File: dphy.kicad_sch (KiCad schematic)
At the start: 5 parts, among them J1002 FFC-22p-P0.5mm, U1002 RCLAMP0524P, U1003 RCLAMP0524P, U1004 RCLAMP0524P, U1005 RCLAMP0524P

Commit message: Fix schematic ERC errors
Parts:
- U1002, U1003, U1004, U1005: footprint Package_SON:USON-10_2.5x1.0mm_P0.5mm -> Package_DFN_QFN:Diodes_UDFN-10_1.0x2.5mm_P0.5mm; symbol Yellow:TPD4EUSB30 -> Hatlabs:RCLAMP0524P
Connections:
- net +3.3V: no longer U1005.7 (D2+)
- net CAM_GPIO0: no longer U1004.7 (D2+)
- net CAM_GPIO1: no longer U1004.6 (D2-)
- net DPHY.C+: no longer U1003.10 (D1+)
- net DPHY.C-: no longer U1003.9 (D1-)
- net DPHY.D0+: no longer U1002.10 (D1+)
- net DPHY.D0-: no longer U1002.9 (D1-)
- net DPHY.D1+: no longer U1002.7 (D2+)
- net DPHY.D1-: no longer U1002.6 (D2-)
- net DPHY.D2+: no longer U1003.7 (D2+)
- net DPHY.D2-: no longer U1003.6 (D2-)
- net DPHY.D3+: no longer U1004.10 (D1+)
- net DPHY.D3-: no longer U1004.9 (D1-)
- net I2C.SCL: no longer U1005.10 (D1+)
- net I2C.SDA: no longer U1005.9 (D1-)
- net at U1005.5: no longer U1005.6 (D2-)
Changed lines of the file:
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@@
 	)
 	(symbol
-		(lib_name "Power_Protection:TPD4EUSB30_1")
-		(lib_id "Yellow:TPD4EUSB30")
+		(lib_id "Hatlabs:RCLAMP0524P")
 		(at 90.17 138.43 0)
 		(unit 1)
@@
 			)
 		)
-		(property "Footprint" "Package_SON:USON-10_2.5x1.0mm_P0.5mm"
+		(property "Footprint" "Package_DFN_QFN:Diodes_UDFN-10_1.0x2.5mm_P0.5mm"
 			(at 66.04 148.59 0)
 			(effects
@@
 			)
 		)
-		(property "Description" ""
+		(property "Description" "4-Channel Low Capacitance TVS Diode Array, DFN-10"
 			(at 90.17 138.43 0)
 			(effects
@@
 					(size 1.27 1.27)
 				)
-			)
-		)
-		(property "Sim.Enable" ""
-			(at 90.17 138.43 0)
-			(effects
-				(font
-					(size 1.27 1.27)
-				)
+				(hide yes)
 			)
 		)
@@
 	)
 	(symbol
-		(lib_name "Power_Protection:TPD4EUSB30_1")
-		(lib_id "Yellow:TPD4EUSB30")
+		(lib_id "Hatlabs:RCLAMP0524P")
 		(at 90.17 73.66 0)
 		(unit 1)
@@
 			)
 		)
-		(property "Footprint" "Package_SON:USON-10_2.5x1.0mm_P0.5mm"
+		(property "Footprint" "Package_DFN_QFN:Diodes_UDFN-10_1.0x2.5mm_P0.5mm"
 			(at 66.04 83.82 0)
 			(effects
@@
 			)
 		)
-		(property "Description" ""
+		(property "Description" "4-Channel Low Capacitance TVS Diode Array, DFN-10"
 			(at 90.17 73.66 0)
 			(effects
@@
 					(size 1.27 1.27)
 				)
-			)
-		)
-		(property "Sim.Enable" ""
-			(at 90.17 73.66 0)
-			(effects
-				(font
-					(size 1.27 1.27)
-				)
+				(hide yes)
 			)
 		)
@@
 	)
 	(symbol
-		(lib_name "Power_Protection:TPD4EUSB30_1")
-		(lib_id "Yellow:TPD4EUSB30")
+		(lib_id "Hatlabs:RCLAMP0524P")
 		(at 90.17 41.91 0)
 		(unit 1)
@@
 			)
 		)
-		(property "Footprint" "Package_SON:USON-10_2.5x1.0mm_P0.5mm"
+		(property "Footprint" "Package_DFN_QFN:Diodes_UDFN-10_1.0x2.5mm_P0.5mm"
 			(at 66.04 52.07 0)
 			(effects
@@
 			)
 		)
-		(property "Description" ""
+		(property "Description" "4-Channel Low Capacitance TVS Diode Array, DFN-10"
 			(at 90.17 41.91 0)
 			(effects
@@
 					(size 1.27 1.27)
 				)
-			)
-		)
-		(property "Sim.Enable" ""
-			(at 90.17 41.91 0)
-			(effects
-				(font
-					(size 1.27 1.27)
-				)
+				(hide yes)
 			)
 		)
@@
 			)
 		)
-		(property "Sim.Enable" ""
-			(at 214.63 91.44 0)
-			(effects
-				(font
-					(size 1.27 1.27)
-				)
-			)
-		)
 		(pin "1"
 		)
@@
 	)
 	(symbol
-		(lib_name "Power_Protection:TPD4EUSB30_1")
-		(lib_id "Yellow:TPD4EUSB30")
+		(lib_id "Hatlabs:RCLAMP0524P")
 		(at 90.17 106.68 0)
 		(unit 1)
@@
 			)
 		)
-		(property "Footprint" "Package_SON:USON-10_2.5x1.0mm_P0.5mm"
+		(property "Footprint" "Package_DFN_QFN:Diodes_UDFN-10_1.0x2.5mm_P0.5mm"
 			(at 66.04 116.84 0)
 			(effects
@@
 			)
 		)
-		(property "Description" ""
+		(property "Description" "4-Channel Low Capacitance TVS Diode Array, DFN-10"
 			(at 90.17 106.68 0)
 			(effects
@@
 					(size 1.27 1.27)
 				)
-			)
-		)
-		(property "Sim.Enable" ""
-			(at 90.17 106.68 0)
-			(effects
-				(font
-					(size 1.27 1.27)
-				)
-			)
-		)
+				(hide yes)
+			)
+		)

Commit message: Renumber all sheets
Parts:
- renumbered J1002 to J3401, U1003 to U3401, U1004 to U3402, U1005 to U3403, U1002 to U3404
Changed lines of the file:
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@@
 		(on_board yes)
 		(dnp no)
-		(property "Reference" "#PWR01014"
+		(property "Reference" "#PWR03402"
 			(at 207.01 127 0)
 			(effects
@@
 		(on_board yes)
 		(dnp no)
-		(property "Reference" "#PWR01010"
+		(property "Reference" "#PWR03405"
 			(at 90.17 92.71 0)
 			(effects
@@
 		(on_board yes)
 		(dnp no)
-		(property "Reference" "#PWR01009"
+		(property "Reference" "#PWR03404"
 			(at 90.17 60.96 0)
 			(effects
@@
 		(on_board yes)
 		(dnp no)
-		(property "Reference" "U1005"
+		(property "Reference" "U3403"
 			(at 90.17 125.73 0)
 			(effects
@@
 		(dnp no)
 		(fields_autoplaced yes)
-		(property "Reference" "#PWR01013"
+		(property "Reference" "#PWR01017"
 			(at 104.14 138.43 0)
 			(effects
@@
 		(on_board yes)
 		(dnp no)
-		(property "Reference" "U1003"
+		(property "Reference" "U3401"
 			(at 90.17 60.96 0)
 			(effects
@@
 		(on_board yes)
 		(dnp no)
-		(property "Reference" "#PWR01011"
+		(property "Reference" "#PWR03406"
 			(at 90.17 125.73 0)
 			(effects
@@
 		(on_board yes)
 		(dnp no)
-		(property "Reference" "#PWR01012"
+		(property "Reference" "#PWR03407"
 			(at 90.17 157.48 0)
 			(effects
@@
 		(on_board yes)
 		(dnp no)
-		(property "Reference" "U1002"
+		(property "Reference" "U3404"
 			(at 90.17 29.21 0)
 			(effects
@@
 		(on_board yes)
 		(dnp no)
-		(property "Reference" "#PWR01015"
+		(property "Reference" "#PWR03403"
 			(at 214.63 130.81 0)
 			(effects
@@
 		(dnp no)
 		(fields_autoplaced yes)
-		(property "Reference" "J1002"
+		(property "Reference" "J3401"
 			(at 217.17 91.7955 0)
 			(effects
@@
 					(size 1.27 1.27)
 				)
+				(hide yes)
 			)
 		)
@@
 		(on_board yes)
 		(dnp no)
-		(property "Reference" "U1004"
+		(property "Reference" "U3402"
 			(at 90.17 93.98 0)
 			(effects
@@
 		(dnp no)
 		(fields_autoplaced yes)
-		(property "Reference" "#PWR01003"
+		(property "Reference" "#PWR03408"
 			(at 186.69 123.19 0)
 			(effects

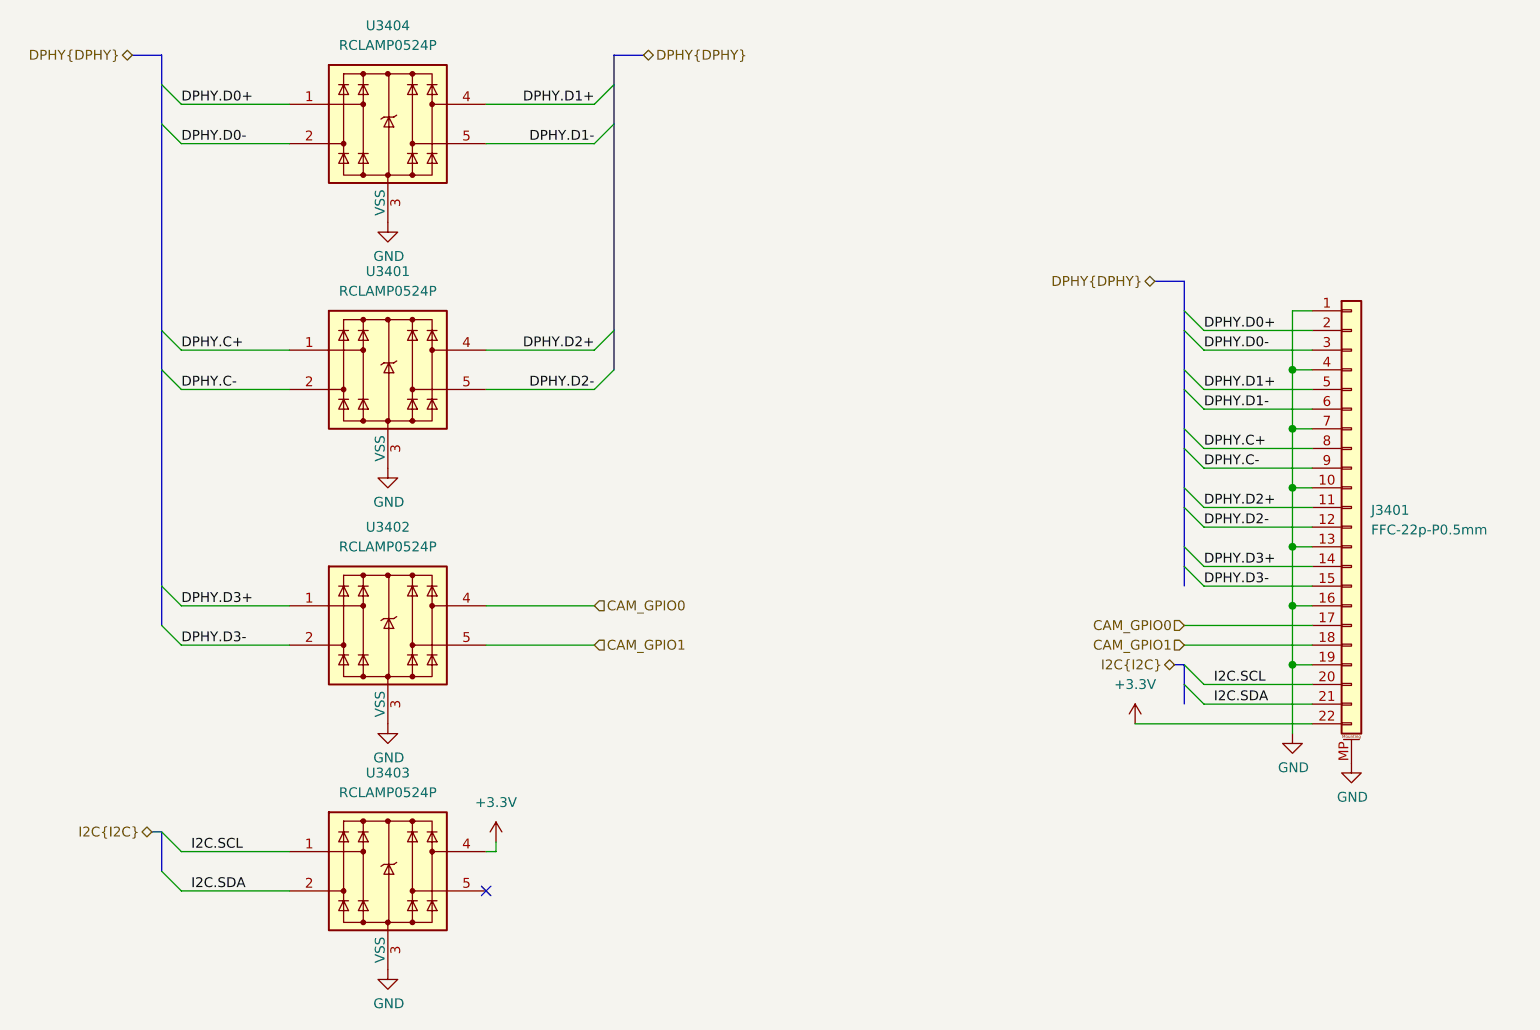
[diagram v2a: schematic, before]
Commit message: Reannotate components
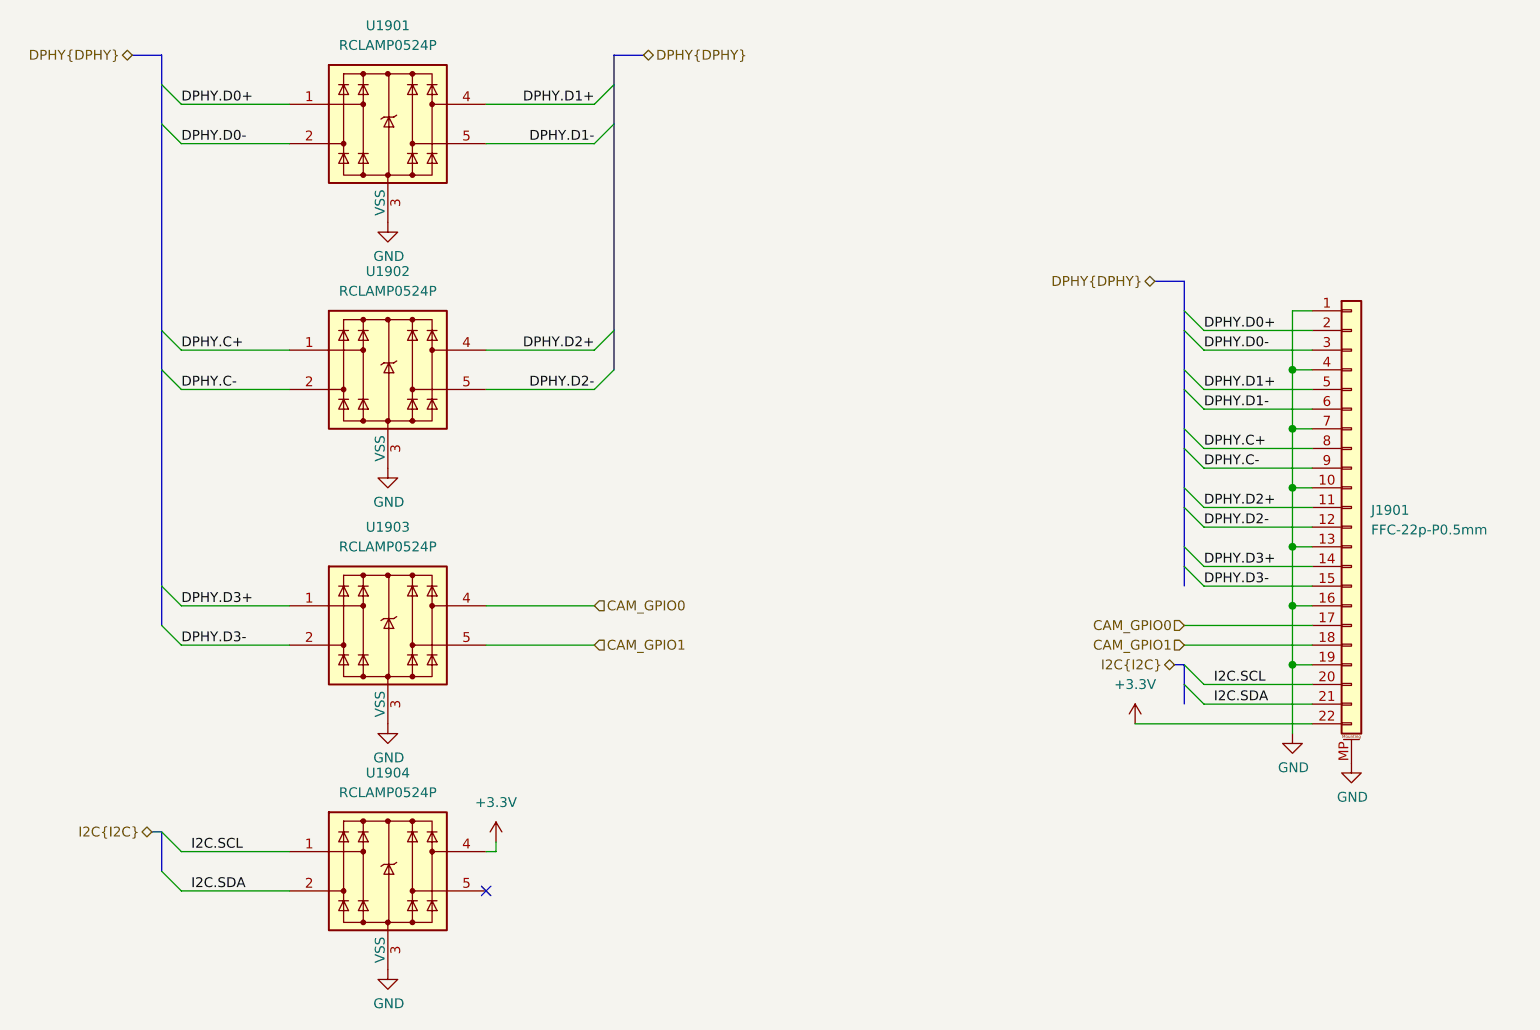
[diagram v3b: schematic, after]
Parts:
- renumbered J3401 to J1901, U3404 to U1901, U3401 to U1902, U3402 to U1903, U3403 to U1904
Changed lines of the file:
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@@
 		(on_board yes)
 		(dnp no)
-		(property "Reference" "#PWR03402"
+		(property "Reference" "#PWR01907"
 			(at 207.01 127 0)
 			(effects
@@
 			(project "HALPI2"
 				(path "/abc482bd-3f17-4d35-80db-1da3dcdb5c27/851e7ce4-d5b0-47f7-ace9-4a347f172348/10568cce-38f9-4351-82fd-0cb3bf8ca49d"
-					(reference "#PWR03402")
-					(unit 1)
-				)
-				(path "/abc482bd-3f17-4d35-80db-1da3dcdb5c27/851e7ce4-d5b0-47f7-ace9-4a347f172348/d4876730-9038-4f8b-92bc-bcbb3a62ccf0"
-					(reference "#PWR01014")
+					(reference "#PWR01907")
+					(unit 1)
+				)
+				(path "/abc482bd-3f17-4d35-80db-1da3dcdb5c27/851e7ce4-d5b0-47f7-ace9-4a347f172348/d4876730-9038-4f8b-92bc-bcbb3a62ccf0"
+					(reference "#PWR02007")
 					(unit 1)
 				)
@@
 		(on_board yes)
 		(dnp no)
-		(property "Reference" "#PWR03405"
+		(property "Reference" "#PWR01902"
 			(at 90.17 92.71 0)
 			(effects
@@
 			(project "HALPI2"
 				(path "/abc482bd-3f17-4d35-80db-1da3dcdb5c27/851e7ce4-d5b0-47f7-ace9-4a347f172348/10568cce-38f9-4351-82fd-0cb3bf8ca49d"
-					(reference "#PWR03405")
-					(unit 1)
-				)
-				(path "/abc482bd-3f17-4d35-80db-1da3dcdb5c27/851e7ce4-d5b0-47f7-ace9-4a347f172348/d4876730-9038-4f8b-92bc-bcbb3a62ccf0"
-					(reference "#PWR01010")
+					(reference "#PWR01902")
+					(unit 1)
+				)
+				(path "/abc482bd-3f17-4d35-80db-1da3dcdb5c27/851e7ce4-d5b0-47f7-ace9-4a347f172348/d4876730-9038-4f8b-92bc-bcbb3a62ccf0"
+					(reference "#PWR02002")
 					(unit 1)
 				)
@@
 		(on_board yes)
 		(dnp no)
-		(property "Reference" "#PWR03404"
+		(property "Reference" "#PWR01901"
 			(at 90.17 60.96 0)
 			(effects
@@
 			(project "HALPI2"
 				(path "/abc482bd-3f17-4d35-80db-1da3dcdb5c27/851e7ce4-d5b0-47f7-ace9-4a347f172348/10568cce-38f9-4351-82fd-0cb3bf8ca49d"
-					(reference "#PWR03404")
-					(unit 1)
-				)
-				(path "/abc482bd-3f17-4d35-80db-1da3dcdb5c27/851e7ce4-d5b0-47f7-ace9-4a347f172348/d4876730-9038-4f8b-92bc-bcbb3a62ccf0"
-					(reference "#PWR01009")
+					(reference "#PWR01901")
+					(unit 1)
+				)
+				(path "/abc482bd-3f17-4d35-80db-1da3dcdb5c27/851e7ce4-d5b0-47f7-ace9-4a347f172348/d4876730-9038-4f8b-92bc-bcbb3a62ccf0"
+					(reference "#PWR02001")
 					(unit 1)
 				)
@@
 		(on_board yes)
 		(dnp no)
-		(property "Reference" "U3403"
+		(property "Reference" "U1904"
 			(at 90.17 125.73 0)
 			(effects
@@
 			(project "HALPI2"
 				(path "/abc482bd-3f17-4d35-80db-1da3dcdb5c27/851e7ce4-d5b0-47f7-ace9-4a347f172348/10568cce-38f9-4351-82fd-0cb3bf8ca49d"
-					(reference "U3403")
-					(unit 1)
-				)
-				(path "/abc482bd-3f17-4d35-80db-1da3dcdb5c27/851e7ce4-d5b0-47f7-ace9-4a347f172348/d4876730-9038-4f8b-92bc-bcbb3a62ccf0"
-					(reference "U1005")
+					(reference "U1904")
+					(unit 1)
+				)
+				(path "/abc482bd-3f17-4d35-80db-1da3dcdb5c27/851e7ce4-d5b0-47f7-ace9-4a347f172348/d4876730-9038-4f8b-92bc-bcbb3a62ccf0"
+					(reference "U2004")
 					(unit 1)
 				)
@@
 		(dnp no)
 		(fields_autoplaced yes)
-		(property "Reference" "#PWR01017"
+		(property "Reference" "#PWR01905"
 			(at 104.14 138.43 0)
 			(effects
@@
 			(project "HALPI2"
 				(path "/abc482bd-3f17-4d35-80db-1da3dcdb5c27/851e7ce4-d5b0-47f7-ace9-4a347f172348/10568cce-38f9-4351-82fd-0cb3bf8ca49d"
-					(reference "#PWR01017")
-					(unit 1)
-				)
-				(path "/abc482bd-3f17-4d35-80db-1da3dcdb5c27/851e7ce4-d5b0-47f7-ace9-4a347f172348/d4876730-9038-4f8b-92bc-bcbb3a62ccf0"
-					(reference "#PWR01013")
+					(reference "#PWR01905")
+					(unit 1)
+				)
+				(path "/abc482bd-3f17-4d35-80db-1da3dcdb5c27/851e7ce4-d5b0-47f7-ace9-4a347f172348/d4876730-9038-4f8b-92bc-bcbb3a62ccf0"
+					(reference "#PWR02005")
 					(unit 1)
 				)
@@
 		(on_board yes)
 		(dnp no)
-		(property "Reference" "U3401"
+		(property "Reference" "U1902"
 			(at 90.17 60.96 0)
 			(effects
@@
 			(project "HALPI2"
 				(path "/abc482bd-3f17-4d35-80db-1da3dcdb5c27/851e7ce4-d5b0-47f7-ace9-4a347f172348/10568cce-38f9-4351-82fd-0cb3bf8ca49d"
-					(reference "U3401")
-					(unit 1)
-				)
-				(path "/abc482bd-3f17-4d35-80db-1da3dcdb5c27/851e7ce4-d5b0-47f7-ace9-4a347f172348/d4876730-9038-4f8b-92bc-bcbb3a62ccf0"
-					(reference "U1003")
+					(reference "U1902")
+					(unit 1)
+				)
+				(path "/abc482bd-3f17-4d35-80db-1da3dcdb5c27/851e7ce4-d5b0-47f7-ace9-4a347f172348/d4876730-9038-4f8b-92bc-bcbb3a62ccf0"
+					(reference "U2002")
 					(unit 1)
 				)
@@
 		(on_board yes)
 		(dnp no)
-		(property "Reference" "#PWR03406"
+		(property "Reference" "#PWR01903"
 			(at 90.17 125.73 0)
 			(effects
@@
 			(project "HALPI2"
 				(path "/abc482bd-3f17-4d35-80db-1da3dcdb5c27/851e7ce4-d5b0-47f7-ace9-4a347f172348/10568cce-38f9-4351-82fd-0cb3bf8ca49d"
-					(reference "#PWR03406")
-					(unit 1)
-				)
-				(path "/abc482bd-3f17-4d35-80db-1da3dcdb5c27/851e7ce4-d5b0-47f7-ace9-4a347f172348/d4876730-9038-4f8b-92bc-bcbb3a62ccf0"
-					(reference "#PWR01011")
+					(reference "#PWR01903")
+					(unit 1)
+				)
+				(path "/abc482bd-3f17-4d35-80db-1da3dcdb5c27/851e7ce4-d5b0-47f7-ace9-4a347f172348/d4876730-9038-4f8b-92bc-bcbb3a62ccf0"
+					(reference "#PWR02003")
 					(unit 1)
 				)
@@
 		(on_board yes)
 		(dnp no)
-		(property "Reference" "#PWR03407"
+		(property "Reference" "#PWR01904"
 			(at 90.17 157.48 0)
 			(effects
@@
 			(project "HALPI2"
 				(path "/abc482bd-3f17-4d35-80db-1da3dcdb5c27/851e7ce4-d5b0-47f7-ace9-4a347f172348/10568cce-38f9-4351-82fd-0cb3bf8ca49d"
-					(reference "#PWR03407")
-					(unit 1)
-				)
-				(path "/abc482bd-3f17-4d35-80db-1da3dcdb5c27/851e7ce4-d5b0-47f7-ace9-4a347f172348/d4876730-9038-4f8b-92bc-bcbb3a62ccf0"
-					(reference "#PWR01012")
+					(reference "#PWR01904")
+					(unit 1)
+				)
+				(path "/abc482bd-3f17-4d35-80db-1da3dcdb5c27/851e7ce4-d5b0-47f7-ace9-4a347f172348/d4876730-9038-4f8b-92bc-bcbb3a62ccf0"
+					(reference "#PWR02004")
 					(unit 1)
 				)
@@
 		(on_board yes)
 		(dnp no)
-		(property "Reference" "U3404"
+		(property "Reference" "U1901"
 			(at 90.17 29.21 0)
 			(effects
@@
 			(project "HALPI2"
 				(path "/abc482bd-3f17-4d35-80db-1da3dcdb5c27/851e7ce4-d5b0-47f7-ace9-4a347f172348/10568cce-38f9-4351-82fd-0cb3bf8ca49d"
-					(reference "U3404")
-					(unit 1)
-				)
-				(path "/abc482bd-3f17-4d35-80db-1da3dcdb5c27/851e7ce4-d5b0-47f7-ace9-4a347f172348/d4876730-9038-4f8b-92bc-bcbb3a62ccf0"
-					(reference "U1002")
+					(reference "U1901")
+					(unit 1)
+				)
+				(path "/abc482bd-3f17-4d35-80db-1da3dcdb5c27/851e7ce4-d5b0-47f7-ace9-4a347f172348/d4876730-9038-4f8b-92bc-bcbb3a62ccf0"
+					(reference "U2001")
 					(unit 1)
 				)
@@
 		(on_board yes)
 		(dnp no)
-		(property "Reference" "#PWR03403"
+		(property "Reference" "#PWR01908"
 			(at 214.63 130.81 0)
 			(effects
@@
 			(project "HALPI2"
 				(path "/abc482bd-3f17-4d35-80db-1da3dcdb5c27/851e7ce4-d5b0-47f7-ace9-4a347f172348/10568cce-38f9-4351-82fd-0cb3bf8ca49d"
-					(reference "#PWR03403")
-					(unit 1)
-				)
-				(path "/abc482bd-3f17-4d35-80db-1da3dcdb5c27/851e7ce4-d5b0-47f7-ace9-4a347f172348/d4876730-9038-4f8b-92bc-bcbb3a62ccf0"
-					(reference "#PWR01015")
+					(reference "#PWR01908")
+					(unit 1)
+				)
+				(path "/abc482bd-3f17-4d35-80db-1da3dcdb5c27/851e7ce4-d5b0-47f7-ace9-4a347f172348/d4876730-9038-4f8b-92bc-bcbb3a62ccf0"
+					(reference "#PWR02008")
 					(unit 1)
 				)
@@
 		(dnp no)
 		(fields_autoplaced yes)
-		(property "Reference" "J3401"
+		(property "Reference" "J1901"
 			(at 217.17 91.7955 0)
 			(effects
@@
 				)
 				(path "/abc482bd-3f17-4d35-80db-1da3dcdb5c27/851e7ce4-d5b0-47f7-ace9-4a347f172348/10568cce-38f9-4351-82fd-0cb3bf8ca49d"
-					(reference "J3401")
-					(unit 1)
-				)
-				(path "/abc482bd-3f17-4d35-80db-1da3dcdb5c27/851e7ce4-d5b0-47f7-ace9-4a347f172348/d4876730-9038-4f8b-92bc-bcbb3a62ccf0"
-					(reference "J1002")
+					(reference "J1901")
+					(unit 1)
+				)
+				(path "/abc482bd-3f17-4d35-80db-1da3dcdb5c27/851e7ce4-d5b0-47f7-ace9-4a347f172348/d4876730-9038-4f8b-92bc-bcbb3a62ccf0"
+					(reference "J2001")
 					(unit 1)
 				)
@@
 		(on_board yes)
 		(dnp no)
-		(property "Reference" "U3402"
+		(property "Reference" "U1903"
 			(at 90.17 93.98 0)
 			(effects
@@
 			(project "HALPI2"
 				(path "/abc482bd-3f17-4d35-80db-1da3dcdb5c27/851e7ce4-d5b0-47f7-ace9-4a347f172348/10568cce-38f9-4351-82fd-0cb3bf8ca49d"
-					(reference "U3402")
-					(unit 1)
-				)
-				(path "/abc482bd-3f17-4d35-80db-1da3dcdb5c27/851e7ce4-d5b0-47f7-ace9-4a347f172348/d4876730-9038-4f8b-92bc-bcbb3a62ccf0"
-					(reference "U1004")
+					(reference "U1903")
+					(unit 1)
+				)
+				(path "/abc482bd-3f17-4d35-80db-1da3dcdb5c27/851e7ce4-d5b0-47f7-ace9-4a347f172348/d4876730-9038-4f8b-92bc-bcbb3a62ccf0"
+					(reference "U2003")
 					(unit 1)
 				)
@@
 		(dnp no)
 		(fields_autoplaced yes)
-		(property "Reference" "#PWR03408"
+		(property "Reference" "#PWR01906"
 			(at 186.69 123.19 0)
 			(effects
@@
 			(project ""
 				(path "/abc482bd-3f17-4d35-80db-1da3dcdb5c27/851e7ce4-d5b0-47f7-ace9-4a347f172348/10568cce-38f9-4351-82fd-0cb3bf8ca49d"
-					(reference "#PWR03408")
-					(unit 1)
-				)
-				(path "/abc482bd-3f17-4d35-80db-1da3dcdb5c27/851e7ce4-d5b0-47f7-ace9-4a347f172348/d4876730-9038-4f8b-92bc-bcbb3a62ccf0"
-					(reference "#PWR01003")
-					(unit 1)
-				)
+					(reference "#PWR01906")
+					(unit 1)
+				)
+				(path "/abc482bd-3f17-4d35-80db-1da3dcdb5c27/851e7ce4-d5b0-47f7-ace9-4a347f172348/d4876730-9038-4f8b-92bc-bcbb3a62ccf0"
+					(reference "#PWR02006")
+					(unit 1)
+				)

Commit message: Most DRC errors fixed
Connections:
- net +3.3V: now also U1904.7 (NC)
- net CAM_GPIO0: now also U1903.7 (NC)
- net CAM_GPIO1: now also U1903.6 (NC)
- net DPHY.C+: now also U1902.10 (NC)
- net DPHY.C-: now also U1902.9 (NC)
- net DPHY.D0+: now also U1901.10 (NC)
- net DPHY.D0-: now also U1901.9 (NC)
- net DPHY.D1+: now also U1901.7 (NC)
- net DPHY.D1-: now also U1901.6 (NC)
- net DPHY.D2+: now also U1902.7 (NC)
- net DPHY.D2-: now also U1902.6 (NC)
- net DPHY.D3+: now also U1903.10 (NC)
- net DPHY.D3-: now also U1903.9 (NC)
- net I2C.SCL: now also U1904.10 (NC)
- net I2C.SDA: now also U1904.9 (NC)
- net at U1904.5: now also U1904.6 (NC)
